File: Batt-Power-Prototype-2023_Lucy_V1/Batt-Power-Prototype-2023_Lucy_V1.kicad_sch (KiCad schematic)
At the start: 51 parts, among them IC1 ESDALC6V1W5, J1 Conn_01x06_Pin, J1 GPIO, J14 DE9_Receptacle_MountingHoles, J4 USB_B_Micro, J6 Conn_01x09_Socket, J8 OLED, SW1 SW_SPDT, SW2 RESET, U1 STM32L432KCUx, U10 8MHz, U10 MCP2542FD-E/SN, U7 FT234XD-R

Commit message: added a bunch of footprints and other stuff...
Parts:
- removed J1: Conn_01x06_Pin, Connector_PinHeader_2.54mm:PinHeader_1x06_P2.54mm_Vertical, symbol Connector:Conn_01x06_Pin
- removed J6: Conn_01x09_Socket, Connector_Dsub:DSUB-9_Female_Horizontal_P2.77x2.84mm_EdgePinOffset7.70mm_Housed_MountingHolesOffset9.12mm, symbol Connector:Conn_01x09_Socket
- removed JP1: SolderJumper_2_Open, symbol Jumper:SolderJumper_2_Open
- added JP3: SolderJumper_2_Open, symbol Jumper:SolderJumper_2_Open
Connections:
- net +3V3: now also J1.4 (Pin_4), J1.9 (Pin_9)
- net CAN_H: now also J14.7
- net CAN_L: now also J14.2
- net DEBUG_SWCLK: now also J1.6 (Pin_6)
- net DEBUG_SWDIO: now also J1.7 (Pin_7)
- net DEBUG_SWO: now also J1.2 (Pin_2)
- net GND: now also J1.3 (Pin_3), J1.8 (Pin_8), J14.0 (PAD), JP3.2 (B)
- net NRST: now also J1.1 (Pin_1)
- net at J1.10 (Pin_10): now also J1.5 (Pin_5)
- net at J14.5: now also JP3.1 (A)
- no-connect marks 19 -> 18
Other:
- note added: "add the 5v"
- note removed: "Add programming header"
- moved on the sheet: C?, D4, J1, J14, R26, U10

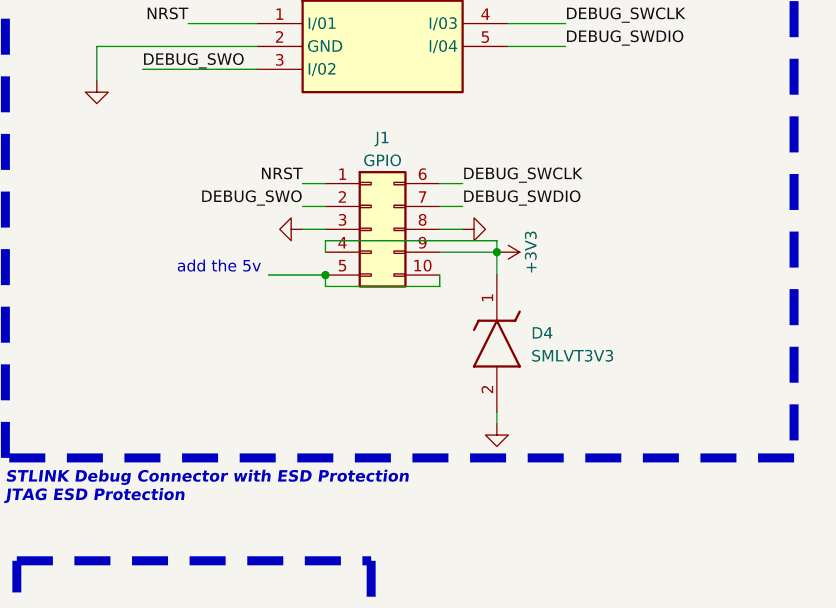
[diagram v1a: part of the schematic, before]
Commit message: added a bunch of foot prints and 3d models
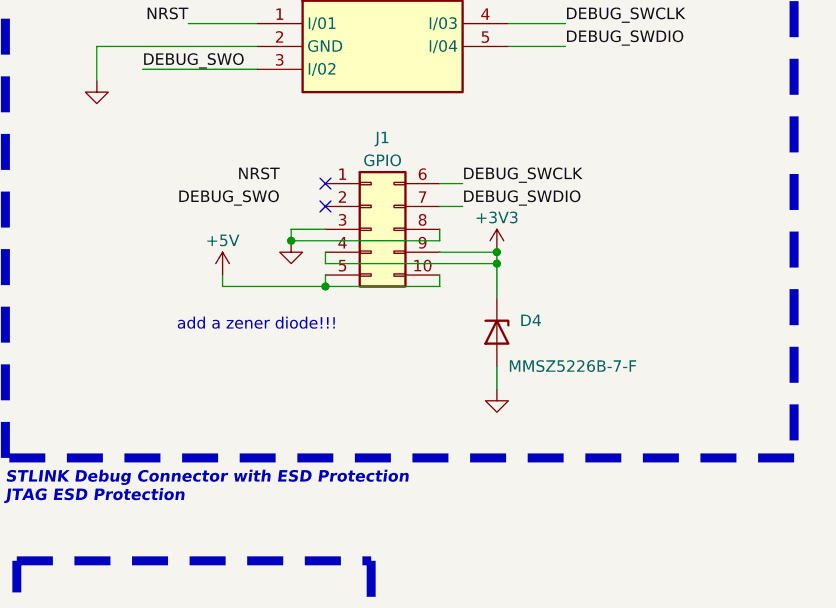
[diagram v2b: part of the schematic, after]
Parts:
- removed D4: SMLVT3V3, SYM&FOOT:DIOM5436X265N, symbol RF_Parts:SMLVT3V3
- added D4: MMSZ5226B-7-F, Diode_SMD:D_SOD-123, symbol Device:D_Zener
- D?: footprint SYM&FOOT:SOT23-6L_STM -> BP_FTP:SOT23-6L_STM-L
- JP3: footprint (none) -> Jumper:SolderJumper-2_P1.3mm_Open_RoundedPad1.0x1.5mm
- U7: footprint digikey-footprints:DFN-12-1EP_3x3mm -> BP_FTP:FT234XD-R
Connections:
- net +3V3: now also D4.1 (K)
- net +5V: now also J1.10 (Pin_10), J1.5 (Pin_5)
- net DEBUG_SWO: no longer J1.2 (Pin_2)
- net GND: now also D4.2 (A)
- net NRST: no longer J1.1 (Pin_1)
- no-connect marks 18 -> 20
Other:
- note added: "add a zener diode!!!"
- note removed: "add the 5v"

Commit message: schematic done??
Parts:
- added D4: MMSZ5231B-7-F, Diode_SMD:D_SOD-123, symbol Device:D_Zener
- IC1: footprint SYM&FOOT:SOT65P210X110-5N -> BP_FTP:SOT65P210X110-5N
- J14: footprint (none) -> Connector_Dsub:DSUB-9_Female_Horizontal_P2.77x2.84mm_EdgePinOffset7.70mm_Housed_MountingHolesOffset9.12mm
- J8: footprint SYM&FOOT:Display_128x64_096_I2C -> BP_FTP:Display_128x64_096_I2C
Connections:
- net +5V: now also D4.1 (K)
- net GND: now also D4.2 (A)
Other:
- note removed: "add a zener diode!!!"
- moved on the sheet: D4, J1, J8

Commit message: made changes to schematic
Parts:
- removed J1: GPIO, Connector_PinHeader_2.54mm:PinHeader_2x05_P2.54mm_Vertical, symbol Connector_Generic:Conn_02x05_Top_Bottom
- J1: symbol Connector_Generic:Conn_02x05_Top_Bottom -> Connector_Generic:Conn_02x05_Odd_Even
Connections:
- net +3V3: now also J1.7 (Pin_7), J1.8 (Pin_8); no longer J1.4 (Pin_4), J1.9 (Pin_9)
- net +5V: now also J1.9 (Pin_9); no longer J1.5 (Pin_5)
- net DEBUG_SWCLK: now also J1.2 (Pin_2); no longer J1.6 (Pin_6)
- net DEBUG_SWDIO: now also J1.4 (Pin_4); no longer J1.7 (Pin_7)
- net GND: now also J1.5 (Pin_5), J1.6 (Pin_6); no longer J1.3 (Pin_3), J1.8 (Pin_8)
- net Battery_Current renamed Battery_Curr
- no-connect marks 20 -> 19
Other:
- sheet Power ports: added Battery_Current; removed none
- note removed: "GPIO"
- moved on the sheet: SW2

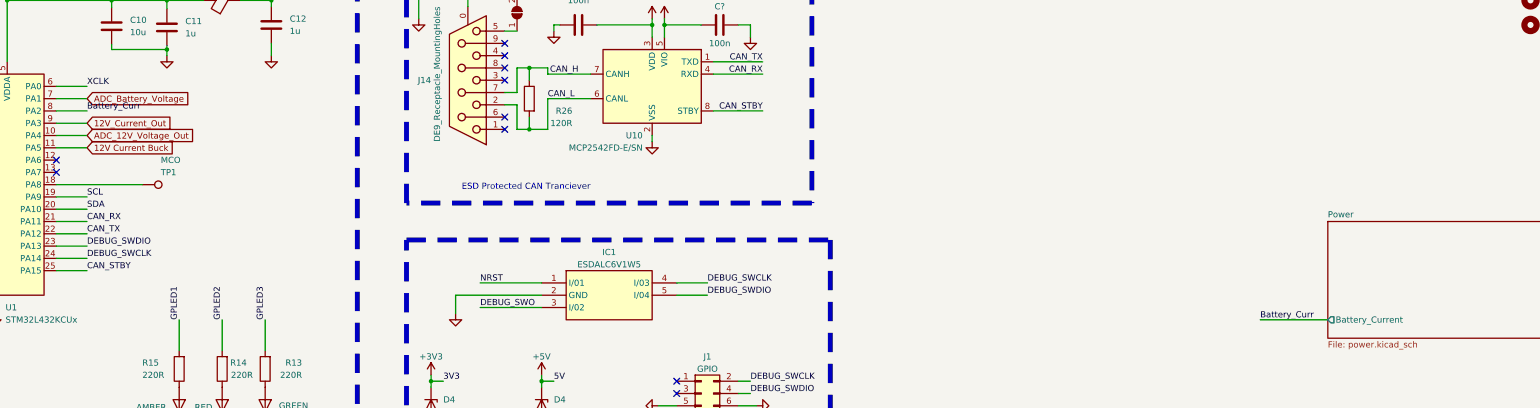
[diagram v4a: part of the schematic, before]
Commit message: no more global variables
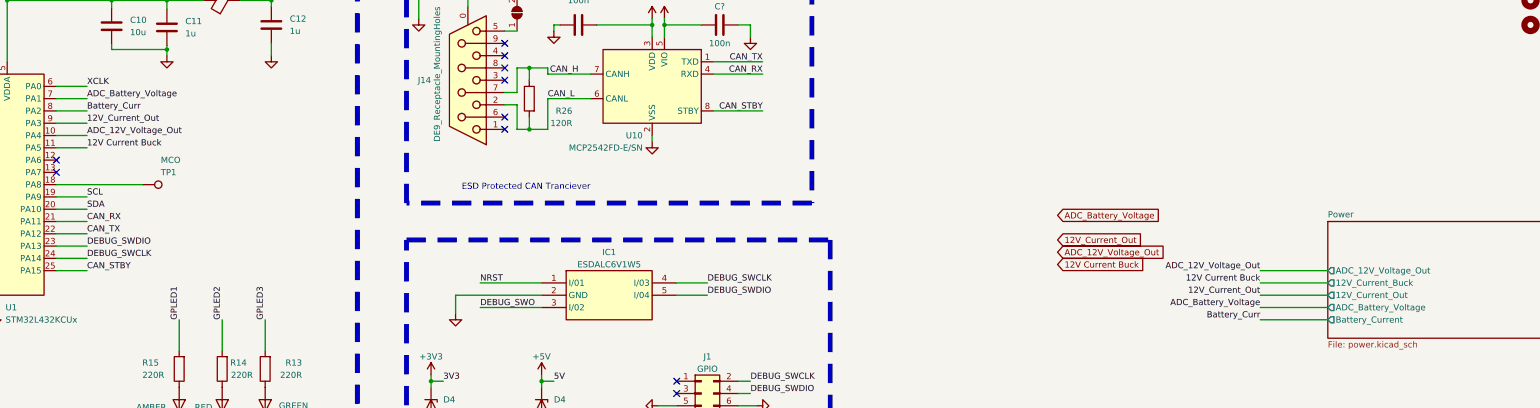
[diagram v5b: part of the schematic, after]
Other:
- sheet Power ports: added 12V_Current_Buck, 12V_Current_Out, ADC_12V_Voltage_Out, ADC_Battery_Voltage; removed none
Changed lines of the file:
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@@
     (stroke (width 0) (type default))
   )
+  (wire (pts (xy 332.74 87.63) (xy 346.71 87.63))
+    (stroke (width 0) (type default))
+  )
   (wire (pts (xy 31.75 165.1) (xy 30.48 165.1))
     (stroke (width 0) (type default))
@@
     (stroke (width 0) (type default))
   )
+  (wire (pts (xy 332.74 85.09) (xy 346.71 85.09))
+    (stroke (width 0) (type default))
+  )
   (wire (pts (xy 38.608 120.904) (xy 38.608 122.174))
     (stroke (width 0) (type default))
@@
     (stroke (width 0) (type default))
   )
+  (wire (pts (xy 332.74 90.17) (xy 346.71 90.17))
+    (stroke (width 0) (type default))
+  )
   (wire (pts (xy 184.15 116.84) (xy 184.15 119.38))
     (stroke (width 0) (type default))
@@
     (stroke (width 0) (type default))
   )
+  (wire (pts (xy 332.74 92.71) (xy 346.71 92.71))
+    (stroke (width 0) (type default))
+  )
   (wire (pts (xy 68.58 29.21) (xy 68.58 40.64))
     (stroke (width 0) (type default))
@@
     (effects (font (size 1.27 1.27)) (justify left bottom))
   )
+  (label "12V_Current_Out" (at 90.17 54.61 0) (fields_autoplaced)
+    (effects (font (size 1.27 1.27)) (justify left bottom))
+  )
   (label "CAN_STBY" (at 229.87 52.07 180) (fields_autoplaced)
     (effects (font (size 1.27 1.27)) (justify right bottom))
@@
     (effects (font (size 1.27 1.27)) (justify right bottom))
   )
+  (label "ADC_Battery_Voltage" (at 332.74 92.71 180) (fields_autoplaced)
+    (effects (font (size 1.27 1.27)) (justify right bottom))
+  )
   (label "GPLED3" (at 127 95.25 90) (fields_autoplaced)
     (effects (font (size 1.27 1.27)) (justify left bottom))
@@
     (effects (font (size 1.27 1.27)) (justify left bottom))
   )
+  (label "12V Current Buck" (at 90.17 59.69 0) (fields_autoplaced)
+    (effects (font (size 1.27 1.27)) (justify left bottom))
+  )
+  (label "ADC_12V_Voltage_Out" (at 332.74 85.09 180) (fields_autoplaced)
+    (effects (font (size 1.27 1.27)) (justify right bottom))
+  )
   (label "DEBUG_SWDIO" (at 90.17 80.01 0) (fields_autoplaced)
     (effects (font (size 1.27 1.27)) (justify left bottom))
@@
     (effects (font (size 1.27 1.27)) (justify left bottom))
   )
+  (label "12V Current Buck" (at 332.74 87.63 180) (fields_autoplaced)
+    (effects (font (size 1.27 1.27)) (justify right bottom))
+  )
   (label "DEBUG_SWDIO" (at 227.33 110.49 0) (fields_autoplaced)
     (effects (font (size 1.27 1.27)) (justify left bottom))
@@
     (effects (font (size 1.27 1.27)) (justify left bottom))
   )
-  (label "Battery_Curr" (at 332.74 95.25 0) (fields_autoplaced)
-    (effects (font (size 1.27 1.27)) (justify left bottom))
+  (label "Battery_Curr" (at 332.74 95.25 180) (fields_autoplaced)
+    (effects (font (size 1.27 1.27)) (justify right bottom))
   )
   (label "UART_TX" (at 53.34 77.47 180) (fields_autoplaced)
@@
     (effects (font (size 1.27 1.27)) (justify left bottom))
   )
+  (label "ADC_12V_Voltage_Out" (at 90.17 57.15 0) (fields_autoplaced)
+    (effects (font (size 1.27 1.27)) (justify left bottom))
+  )
+  (label "ADC_Battery_Voltage" (at 90.17 49.53 0) (fields_autoplaced)
+    (effects (font (size 1.27 1.27)) (justify left bottom))
+  )
   (label "3V3" (at 208.28 115.57 0) (fields_autoplaced)
     (effects (font (size 1.27 1.27)) (justify left bottom))
@@
     (effects (font (size 1.27 1.27)) (justify left bottom))
   )
+  (label "12V_Current_Out" (at 332.74 90.17 180) (fields_autoplaced)
+    (effects (font (size 1.27 1.27)) (justify right bottom))
+  )
   (label "NRST" (at 53.34 46.99 180) (fields_autoplaced)
     (effects (font (size 1.27 1.27)) (justify right bottom))
@@
     (effects (font (size 1.27 1.27)) (justify left bottom))
   )
-  (global_label "12V Current Buck" (shape input) (at 90.17 59.69 0) (fields_autoplaced)
+  (global_label "12V_Current_Out" (shape input) (at 290.83 78.74 0) (fields_autoplaced)
     (effects (font (size 1.27 1.27)) (justify left))
-    (property "Intersheetrefs" "${INTERSHEET_REFS}" (at 110.0884 59.69 0)
+    (property "Intersheetrefs" "${INTERSHEET_REFS}" (at 309.4179 78.74 0)
       (effects (font (size 1.27 1.27)) (justify left) hide)
     )
   )
-  (global_label "ADC_12V_Voltage_Out" (shape input) (at 90.17 57.15 0) (fields_autoplaced)
+  (global_label "12V Current Buck" (shape input) (at 290.83 83.82 0) (fields_autoplaced)
     (effects (font (size 1.27 1.27)) (justify left))
-    (property "Intersheetrefs" "${INTERSHEET_REFS}" (at 113.4145 57.15 0)
+    (property "Intersheetrefs" "${INTERSHEET_REFS}" (at 310.7484 83.82 0)
       (effects (font (size 1.27 1.27)) (justify left) hide)
     )
   )
-  (global_label "12V_Current_Out" (shape input) (at 90.17 54.61 0) (fields_autoplaced)
+  (global_label "ADC_Battery_Voltage" (shape input) (at 290.83 73.66 0) (fields_autoplaced)
     (effects (font (size 1.27 1.27)) (justify left))
-    (property "Intersheetrefs" "${INTERSHEET_REFS}" (at 108.7579 54.61 0)
+    (property "Intersheetrefs" "${INTERSHEET_REFS}" (at 313.1069 73.66 0)
       (effects (font (size 1.27 1.27)) (justify left) hide)
     )
   )
-  (global_label "ADC_Battery_Voltage" (shape input) (at 90.17 49.53 0) (fields_autoplaced)
+  (global_label "ADC_12V_Voltage_Out" (shape input) (at 290.83 81.28 0) (fields_autoplaced)
     (effects (font (size 1.27 1.27)) (justify left))
-    (property "Intersheetrefs" "${INTERSHEET_REFS}" (at 112.4469 49.53 0)
+    (property "Intersheetrefs" "${INTERSHEET_REFS}" (at 314.0745 81.28 0)
       (effects (font (size 1.27 1.27)) (justify left) hide)
     )
@@
       (effects (font (size 1.27 1.27)) (justify left))
     )
+    (pin "ADC_Battery_Voltage" output (at 346.71 92.71 180)
+      (effects (font (size 1.27 1.27)) (justify left))
+    )
+    (pin "ADC_12V_Voltage_Out" output (at 346.71 85.09 180)
+      (effects (font (size 1.27 1.27)) (justify left))
+    )
+    (pin "12V_Current_Buck" output (at 346.71 87.63 180)
+      (effects (font (size 1.27 1.27)) (justify left))
+    )
+    (pin "12V_Current_Out" output (at 346.71 90.17 180)
+      (effects (font (size 1.27 1.27)) (justify left))
+    )

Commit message: some of the touch ups
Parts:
- renumbered C8 to C?, C7 to C?, C15 to C?, C54 to C?, C17 to C?, C1 to C?, C16 to C?, C10 to C?, C11 to C?, C9 to C?, C12 to C?, D8 to D?, D4 to D?, D6 to D?, D7 to D?, D9 to D?, FB1 to FB?, H4 to H?, H3 to H?, H2 to H?, H1 to H?, IC1 to IC?, J14 to J3, J4 to J?, J1 to J?, J8 to J?, JP3 to JP1, R15 to R?, R14 to R?, R26 to R?, R16 to R?, R1 to R?, R13 to R?, SW1 to SW?, SW2 to SW?, TP1 to TP?, U10 to U?, U7 to U?, U1 to U?
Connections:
- net 12V Current Buck renamed 12V_Current_Buck
